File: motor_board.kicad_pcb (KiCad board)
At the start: 2 copper layers, 100 x 100 mm, 34 parts, among them J1 MyRIO_C, J10 ESCON_24-2, J11 Conn_01x02, J12 Conn_01x05, J13 Conn_01x03, J14 BNC, J15 BNC, J16 BNC, J2 BNC, J3 BNC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

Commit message: board v1.1
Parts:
- removed J14, J15, J16: BNC, motor_board:Vertical_BNC_Amphenol_112536
- J2, J3, J4: footprint motor_board:Vertical_BNC_Molex_73131-5003 -> motor_board:Vertical_BNC_Amphenol_112536
- moved J11 37.1 mm to (132.5, 67.5), turned to 90 degrees
- moved R5 26.7 mm to (88.3, 114.2)
- moved R6 26.7 mm to (88.3, 116.8)
- moved D3 8.97 mm to (81.0, 108.8)
- moved R3 7.75 mm to (69.8, 114.2)
- moved R4 7.75 mm to (69.8, 116.8)
- moved F1 6.13 mm to (101.5, 60.5)
- moved J13 6.02 mm to (94.8, 87.8)
- moved JP1 3.76 mm to (95.2, 106.2)
- moved C1 3.55 mm to (99.5, 73.2)
- moved J4 3.40 mm to (90.0, 48.2)
- moved J2 3.01 mm to (49.0, 48.2)
- moved SW1 2.25 mm to (65.5, 128.5)
- moved SW2 2.25 mm to (83.8, 128.5)
- moved J3 2.02 mm to (69.5, 48.2)
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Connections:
- J10 pad 10: (no net) -> unconnected-(J10-A-Pad10)
- J10 pad 11: (no net) -> unconnected-(J10-A\-Pad11)
- J10 pad 12: (no net) -> unconnected-(J10-B-Pad12)
- J10 pad 13: (no net) -> unconnected-(J10-B\-Pad13)
- J10 pad 14: (no net) -> unconnected-(J10-IO4-Pad14)
- J10 pad 15: (no net) -> unconnected-(J10-IO3-Pad15)
- J10 pad 16: (no net) -> unconnected-(J10-IN2-Pad16)
- J10 pad 3: (no net) -> unconnected-(J10-M3-Pad3)
- J10 pad 7: (no net) -> unconnected-(J10-H1-Pad7)
- J10 pad 8: (no net) -> unconnected-(J10-H2-Pad8)
- J10 pad 9: (no net) -> unconnected-(J10-H3-Pad9)
- J12 pad 2: (no net) -> unconnected-(J12-Pin_2-Pad2)
- J6 pad 3: (no net) -> unconnected-(J6-Pad3)
- J8 pad 2: (no net) -> unconnected-(J8-Pin_2-Pad2)
- J9 pad 2: (no net) -> unconnected-(J9-Pin_2-Pad2)
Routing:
- net /M-: track 34.5 -> 75.6 mm
- net /M+: track 44.4 -> 74.7 mm
- net 5V: track 70.2 -> 54.2 mm
- net GNDD: track 158.0 -> 173.8 mm
- net /ENC1.B: track 57.6 -> 65.5 mm
- net /ENC1.A: track 49.1 -> 57.0 mm
- net /AI0-: track 110.1 -> 102.3 mm
- net /PWM: track 127.6 -> 119.9 mm
- net Net-(D2-K): track 80.3 -> 87.6 mm
- net VBUS: track 32.6 -> 26.8 mm
- net /ENC0.B: track 148.2 -> 142.9 mm
- net /AO1: track 100.9 -> 97.4 mm
- net Net-(J10-IN1): track 16.9 -> 13.6 mm
- net /+5: track 39.3 -> 36.1 mm
- net /AI0+: track 79.4 -> 76.9 mm
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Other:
- net class Default removed
- net class Input Power removed
- net class Motor Power removed
- net class MyRIO Power removed
- board text added: "4A Fuse"
- board text added: "Designed By: Cameron Devine September 2023"
- board text added: "Motor"
- board text added: "V1.1"
- board text removed: "Designed By: Cameron Devine April 2023"
- board text removed: "V1.0"

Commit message: fixed the motor label polarity issue
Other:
- board text added: "V1.2"
- board text removed: "V1.1"
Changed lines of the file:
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@@
   (gr_line (start 138 137.25) (end 38 137.25)
     (stroke (width 0.05) (type solid)) (layer "Edge.Cuts"))
-  (gr_text "V1.1" (at 112 51) (layer "B.SilkS")
+  (gr_text "V1.2" (at 112 51) (layer "B.SilkS")
     (effects (font (size 2 2) (thickness 0.3)) (justify mirror))
   )
@@
     (effects (font (size 1.5 1.5) (thickness 0.25)) (justify left))
   )
-  (gr_text "+" (at 127.75 62.25) (layer "F.SilkS")
+  (gr_text "-" (at 127.75 62.25) (layer "F.SilkS")
     (effects (font (size 1.5 1.5) (thickness 0.25)) (justify right))
   )
-  (gr_text "-" (at 127.75 67.25) (layer "F.SilkS")
+  (gr_text "+" (at 127.75 67.25) (layer "F.SilkS")
     (effects (font (size 1.5 1.5) (thickness 0.25)) (justify right))
   )

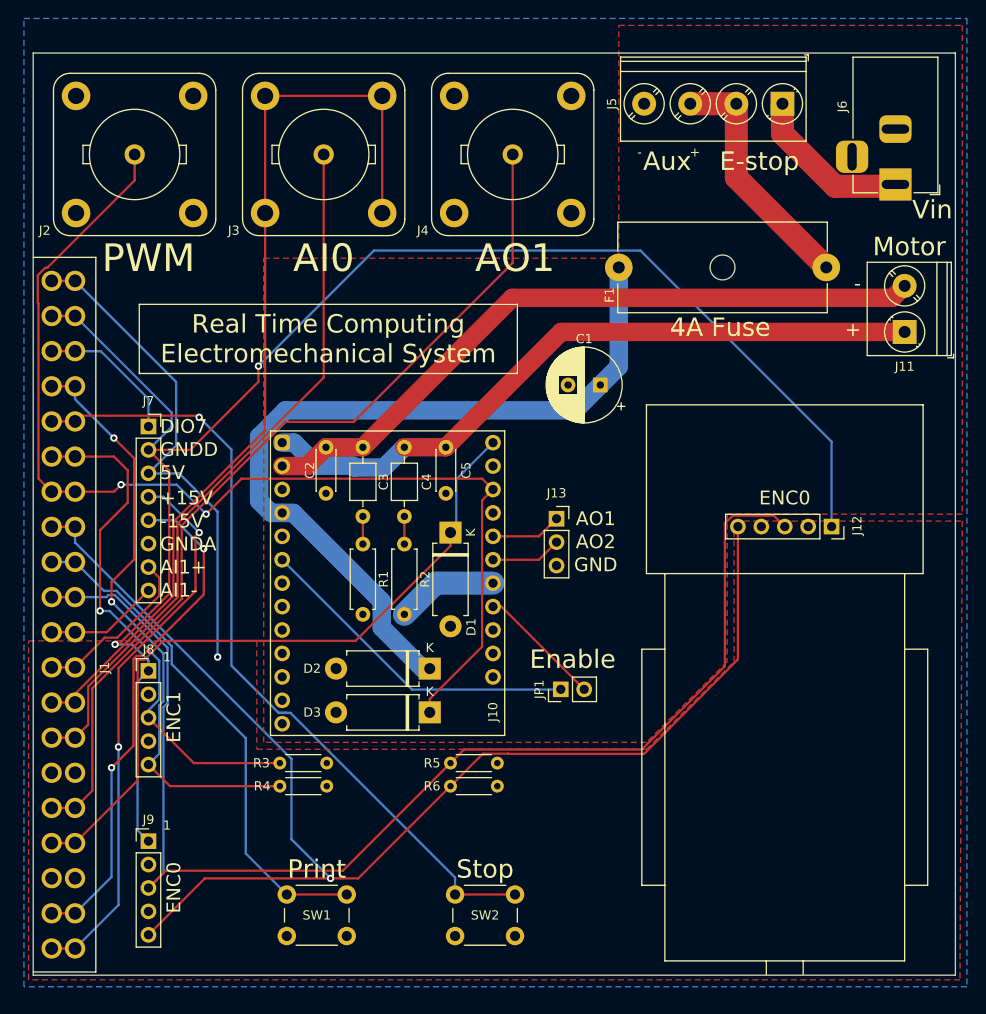
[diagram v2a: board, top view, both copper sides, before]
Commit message: added a couple mounting holes and updated the motor mount
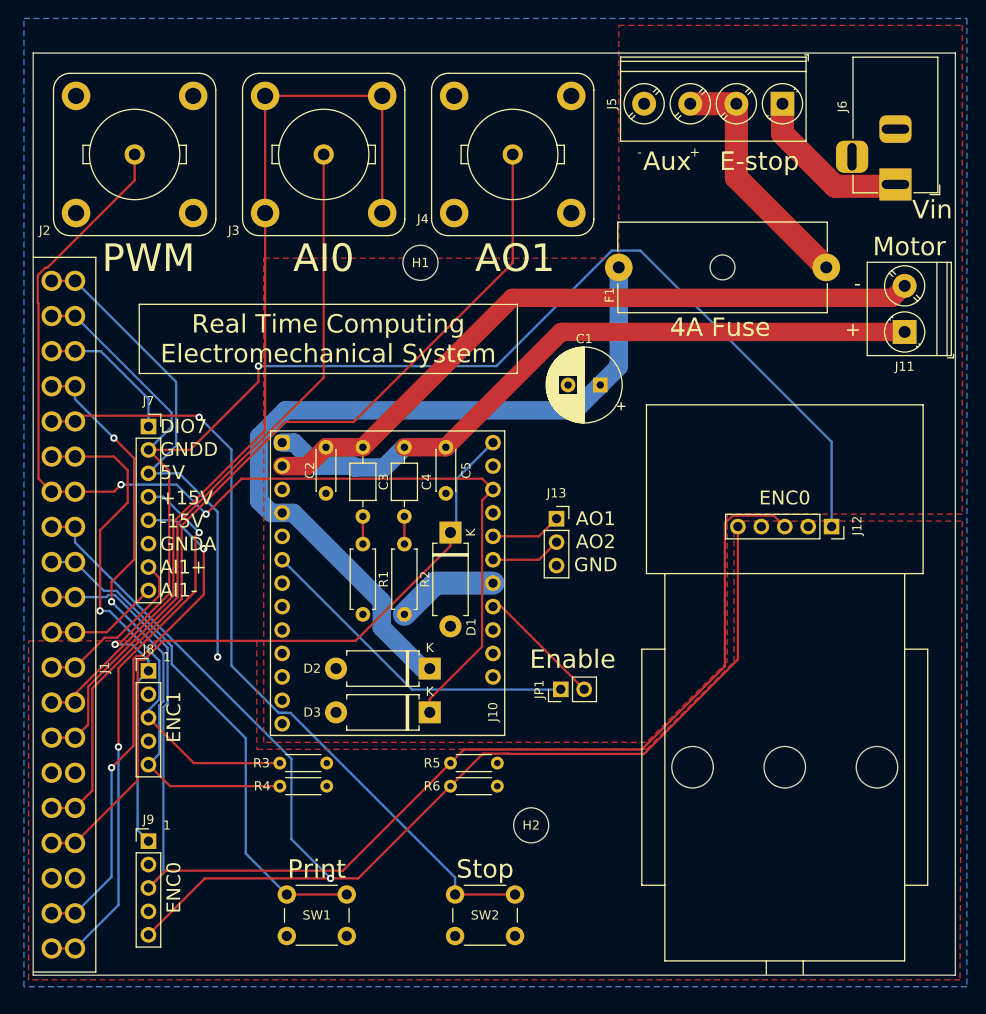
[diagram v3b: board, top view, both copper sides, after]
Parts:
- added H1: MountingHole, motor_board:MountingHole_#6, F.Cu at (80.0, 60.0)
- added H2: MountingHole, motor_board:MountingHole_#6, F.Cu at (92.0, 121.0)
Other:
- board text added: "Designed By: Cameron Devine October 2023"
- board text removed: "Designed By: Cameron Devine September 2023"

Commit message: updated the board with a 90 degree twisted motor and 5 bncs plus amp input switch and trim.
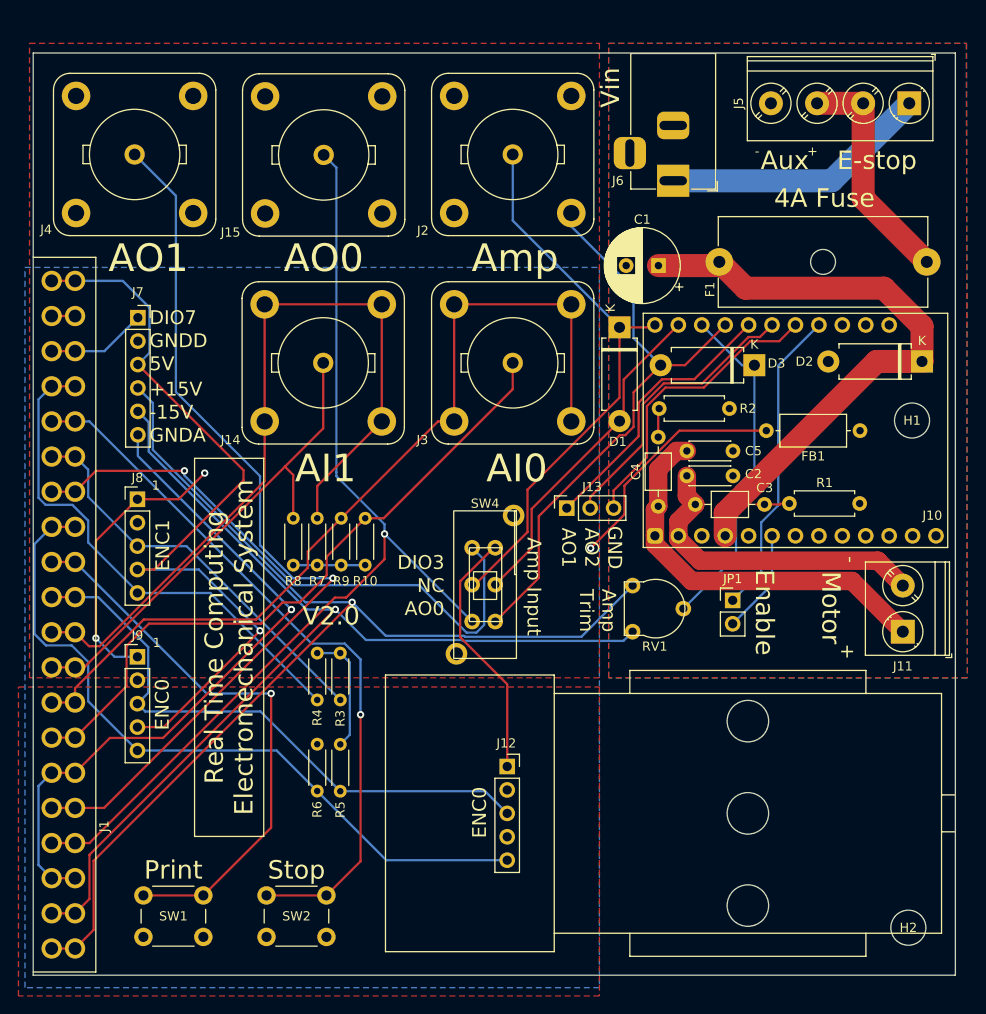
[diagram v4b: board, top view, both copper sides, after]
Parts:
- added FB1: FerriteBead, Inductor_THT:L_Axial_L7.0mm_D3.3mm_P10.16mm_Horizontal_Fastron_MICC, F.Cu at (127.7, 78.2)
- added J14: BNC, motor_board:Vertical_BNC_Amphenol_112536, F.Cu at (69.5, 70.8)
- added J15: BNC, motor_board:Vertical_BNC_Amphenol_112536, F.Cu at (69.5, 48.3)
- added R10: 100k, Resistor_THT:R_Axial_DIN0204_L3.6mm_D1.6mm_P5.08mm_Horizontal, F.Cu at (74.0, 92.8)
- added R7: 100k, Resistor_THT:R_Axial_DIN0204_L3.6mm_D1.6mm_P5.08mm_Horizontal, F.Cu at (68.8, 92.8)
- added R8: 100k, Resistor_THT:R_Axial_DIN0204_L3.6mm_D1.6mm_P5.08mm_Horizontal, F.Cu at (66.2, 92.8)
- added R9: 100k, Resistor_THT:R_Axial_DIN0204_L3.6mm_D1.6mm_P5.08mm_Horizontal, F.Cu at (71.4, 92.8)
- added RV1: 1k, motor_board:CUI PTN06-E Pot, F.Cu at (105.5, 97.5)
- added SW4: SW_DPDT_x2, motor_board:TE Connectivity MHS DPDT Slide Switch, F.Cu at (90.1, 87.4)
- D1, D3: value D_TVS -> P6KE16CA
- J7: value Conn_01x08 -> Conn_01x06; footprint Connector_PinSocket_2.54mm:PinSocket_1x08_P2.54mm_Vertical -> Connector_PinSocket_2.54mm:PinSocket_1x06_P2.54mm_Vertical
- moved D2 62.9 mm to (134.4, 70.7)
- moved H1 56.0 mm to (133.3, 77.1)
- moved J12 54.7 mm to (81.3, 119.7), turned to 0 degrees
- moved D3 51.5 mm to (116.2, 71.1)
- moved R1 46.5 mm to (120.0, 86.1), turned to 0 degrees
- moved H2 42.4 mm to (132.9, 132.1)
- moved J10 41.7 mm to (105.4, 89.6), turned to 180 degrees
- moved J2 41.0 mm to (90.0, 48.2)
- moved J4 41.0 mm to (49.0, 48.2)
- moved C2 39.3 mm to (108.9, 83.1), turned to 0 degrees
- moved C3 36.6 mm to (109.8, 86.2), turned to 0 degrees
- moved J11 32.5 mm to (132.3, 100.0)
- moved R2 31.3 mm to (105.9, 75.8), turned to 0 degrees
- moved J3 30.5 mm to (90.0, 70.8)
- moved D1 28.8 mm to (101.6, 67.0)
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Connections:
- net /AI0+ renamed Net-(J1-AI0+)
- net /AI0- renamed Net-(J1-AI0-)
- net /AO1 renamed Net-(J1-AO1)
- net /BUT1 renamed Net-(J1-DIO1)
- net /BUT2 renamed Net-(J1-DIO5)
- net /DIO7 renamed Net-(J1-DIO7/PWM1)
- net /ENC0.A renamed Net-(J1-DIO0/ENC0.A)
- net /ENC0.B renamed Net-(J1-DIO2/ENC0.B)
- net /ENC1.A renamed Net-(J1-DIO4/ENC1.A)
- net /ENC1.B renamed Net-(J1-DIO6/ENC1.B)
- net /M+ renamed Net-(J10-M+)
- net /M- renamed Net-(J10-M-)
- net 5V renamed Net-(J1-5V)
- net VBUS renamed Net-(J5-Pin_2)
- net VIN renamed Net-(J5-Pin_1)
- D1 pad 1: /CUR -> Net-(D1-A1)
- D1 pad 2: GNDA -> Net-(D1-A2)
- D3 pad 1: /PWM -> Net-(D3-A1)
- J1 pad 10: /AI1- -> Net-(J1-AI1-)
- J1 pad 14: /PWM -> Net-(J1-DIO3/PWM0)
- J1 pad 4: /CUR -> Net-(J1-AO0)
- J1 pad 9: /AI1+ -> Net-(J1-AI1+)
- J10 pad 18: GNDPWR -> GND
- J10 pad 22: /PWM -> Net-(D3-A1)
- J10 pad 23: GNDA -> Net-(D1-A2)
- J10 pad 24: /CUR -> Net-(D1-A1)
- J10 pad 6: /+5 -> Net-(J10-+5)
- J13 pad 3: GNDPWR -> GND
- J2 pad 1: /PWM -> Net-(D1-A1)
- JP1 pad 1: /+5 -> Net-(J10-IN1)
- JP1 pad 2: Net-(J10-IN1) -> Net-(J10-+5)
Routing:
- net GNDA: track 0.00 -> 147.0 mm, vias 0 -> 1
- net /PWM: track 119.9 -> 0.00 mm, vias 2 -> 0
- net Net-(J1-AO0): track 0.00 -> 108.9 mm, vias 0 -> 1
- net Net-(J1-AI1-): track 0.00 -> 89.1 mm
- net GNDD: track 173.8 -> 86.9 mm, vias 2 -> 3
- net /CUR: track 77.3 -> 0.00 mm
- net Net-(J1-DIO0/ENC0.A): track 137.2 -> 64.4 mm
- net Net-(J1-DIO3/PWM0): track 0.00 -> 64.6 mm, vias 0 -> 1
- net Net-(J1-DIO2/ENC0.B): track 142.9 -> 78.8 mm, vias 1 -> 0
- net /+15V: track 60.3 -> 122.6 mm, vias 2 -> 1
- net Net-(D1-A1): track 0.00 -> 62.2 mm
- net /-15V: track 55.5 -> 113.5 mm, vias 2 -> 1
- net Net-(J1-AI1+): track 0.00 -> 53.3 mm
- net Net-(J1-5V): track 54.2 -> 98.2 mm
- net Net-(J10-M-): track 75.6 -> 34.4 mm
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- added copper zone on F.Cu, net GNDA
- added copper zone on B.Cu, net GNDD
- added copper zone on B.Cu, net GNDPWR
- removed copper zone on B.Cu, net GNDA
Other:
- board text added: "AI1"
- board text added: "AO0"
- board text added: "Amp"
- board text added: "Amp Input"
- board text added: "Amp Trim"
- board text added: "DIO3"
- board text added: "NC"
- board text added: "V2.0"
- board text removed: "AI1+"
- board text removed: "AI1-"
- board text removed: "PWM"
- board text removed: "V1.2"

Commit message: got the motor rotated back 90 degrees to its original orientation
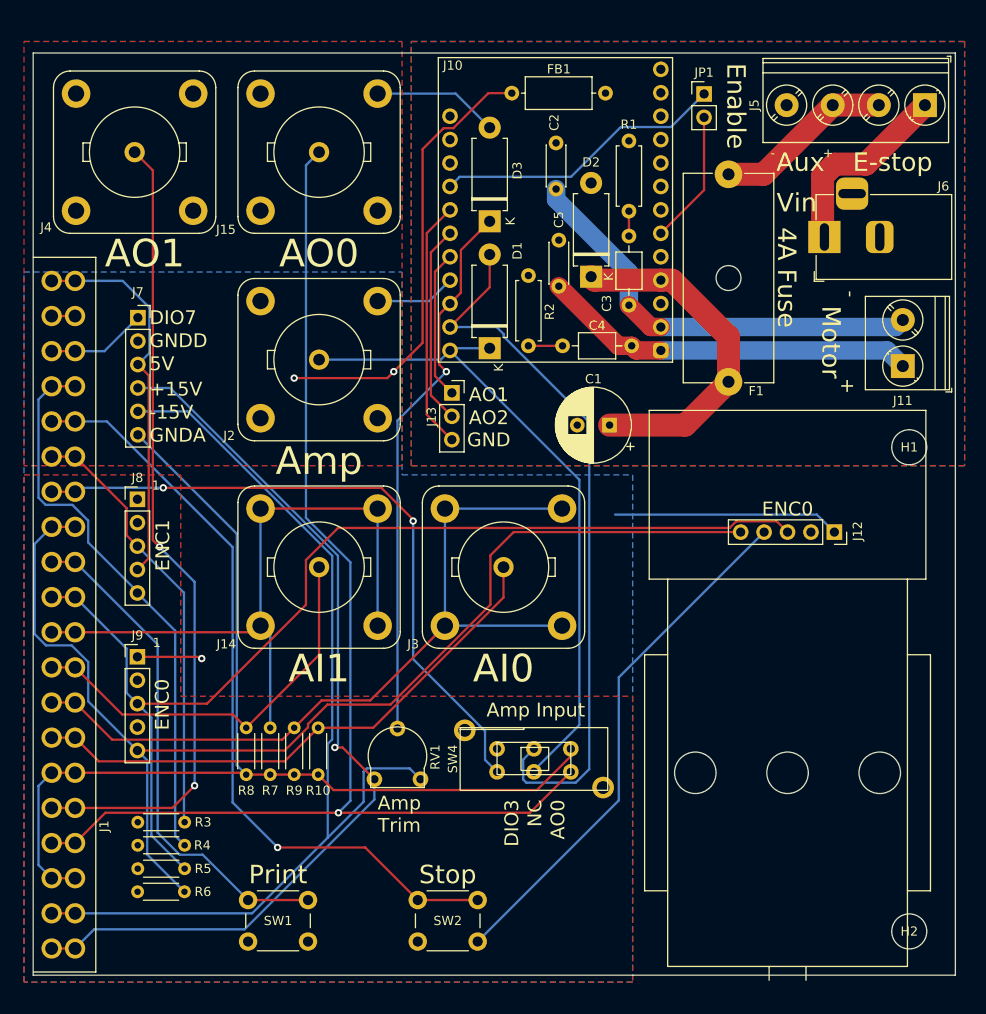
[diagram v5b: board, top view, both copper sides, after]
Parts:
- moved JP1 55.0 mm to (110.8, 41.7)
- moved J12 54.5 mm to (119.8, 81.1), turned to -90 degrees
- moved FB1 45.8 mm to (100.1, 41.6)
- moved D2 37.0 mm to (98.5, 61.5), turned to 90 degrees
- moved R1 36.2 mm to (102.6, 54.4), turned to 90 degrees
- moved C2 34.2 mm to (94.7, 52.0), turned to 90 degrees
- moved D3 32.7 mm to (87.5, 55.5), turned to 90 degrees
- moved RV1 32.2 mm to (77.5, 113.5), turned to 90 degrees
- moved J2 30.6 mm to (69.0, 70.5)
- moved J11 28.8 mm to (132.3, 71.2)
- moved R3 28.6 mm to (49.3, 120.7), turned to 0 degrees
- moved R4 28.5 mm to (49.3, 123.2), turned to 0 degrees
- moved R5 25.8 mm to (49.3, 125.7), turned to 0 degrees
- moved R6 25.2 mm to (49.3, 128.2), turned to 0 degrees
- moved SW4 23.9 mm to (84.8, 110.7), turned to 0 degrees
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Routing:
- net Net-(J1-DIO0/ENC0.A): track 64.4 -> 118.9 mm
- net Net-(J1-DIO2/ENC0.B): track 78.8 -> 129.8 mm
- net Net-(D1-A2): track 36.4 -> 78.5 mm
- net Net-(D2-K): track 66.1 -> 37.3 mm
- net Net-(J1-AO0): track 108.9 -> 134.3 mm
- net /+15V: track 122.6 -> 99.8 mm
- net Net-(D3-A1): track 37.1 -> 59.8 mm, vias 0 -> 1
- net Net-(J1-AI1-): track 89.1 -> 72.5 mm
- net Net-(J10-AO1): track 30.1 -> 16.2 mm
- net Net-(J10-M-): track 34.4 -> 46.9 mm
- net Net-(J1-AI0+): track 72.2 -> 60.7 mm
- net Net-(J1-AO1): track 98.3 -> 87.9 mm, vias 1 -> 2
- net Net-(D1-A1): track 62.2 -> 72.6 mm
- net Net-(J10-AO2): track 31.2 -> 21.6 mm
- net Net-(J1-AI0-): track 96.3 -> 87.5 mm
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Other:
- board text added: "Designed By: Cameron Devine August 2024"
- board text removed: "Designed By: Cameron Devine October 2023"

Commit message: added a resistor divider to the PWM amp input
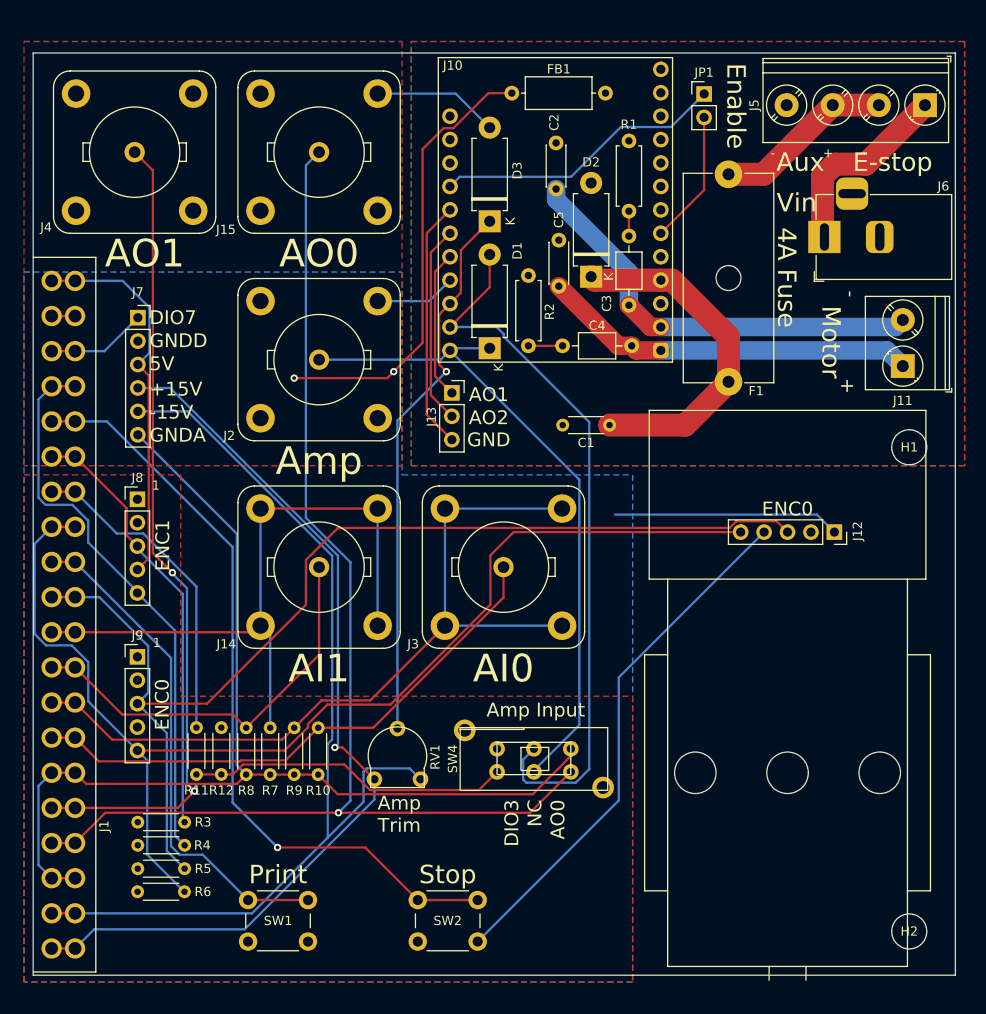
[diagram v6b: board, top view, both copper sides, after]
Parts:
- added R11: 22k, Resistor_THT:R_Axial_DIN0204_L3.6mm_D1.6mm_P5.08mm_Horizontal, F.Cu at (55.7, 115.5)
- added R12: 8.2k, Resistor_THT:R_Axial_DIN0204_L3.6mm_D1.6mm_P5.08mm_Horizontal, F.Cu at (58.4, 115.5)
- C1: footprint Capacitor_THT:CP_Radial_D8.0mm_P3.50mm -> Resistor_THT:R_Axial_DIN0204_L3.6mm_D1.6mm_P5.08mm_Horizontal
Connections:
- SW4 pad 3: Net-(J1-DIO3/PWM0) -> Net-(SW4A-C)
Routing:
- net Net-(J1-DIO3/PWM0): track 71.9 -> 35.8 mm, vias 2 -> 0
- net Net-(SW4A-C): track 0.00 -> 35.0 mm
- net GNDD: track 82.9 -> 75.8 mm, vias 3 -> 2
- net Net-(J1-DIO0/ENC0.A): track 118.9 -> 121.4 mm
- net GNDA: track 138.7 -> 140.2 mm
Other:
- board text added: "V2.1"
- board text removed: "V2.0"
